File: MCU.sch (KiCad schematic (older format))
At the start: 10 parts, among them J2 Conn_01x02, J5 Conn_02x03_Odd_Even, SW2 SW_SPDT, U3 ATTINY13-20SSU

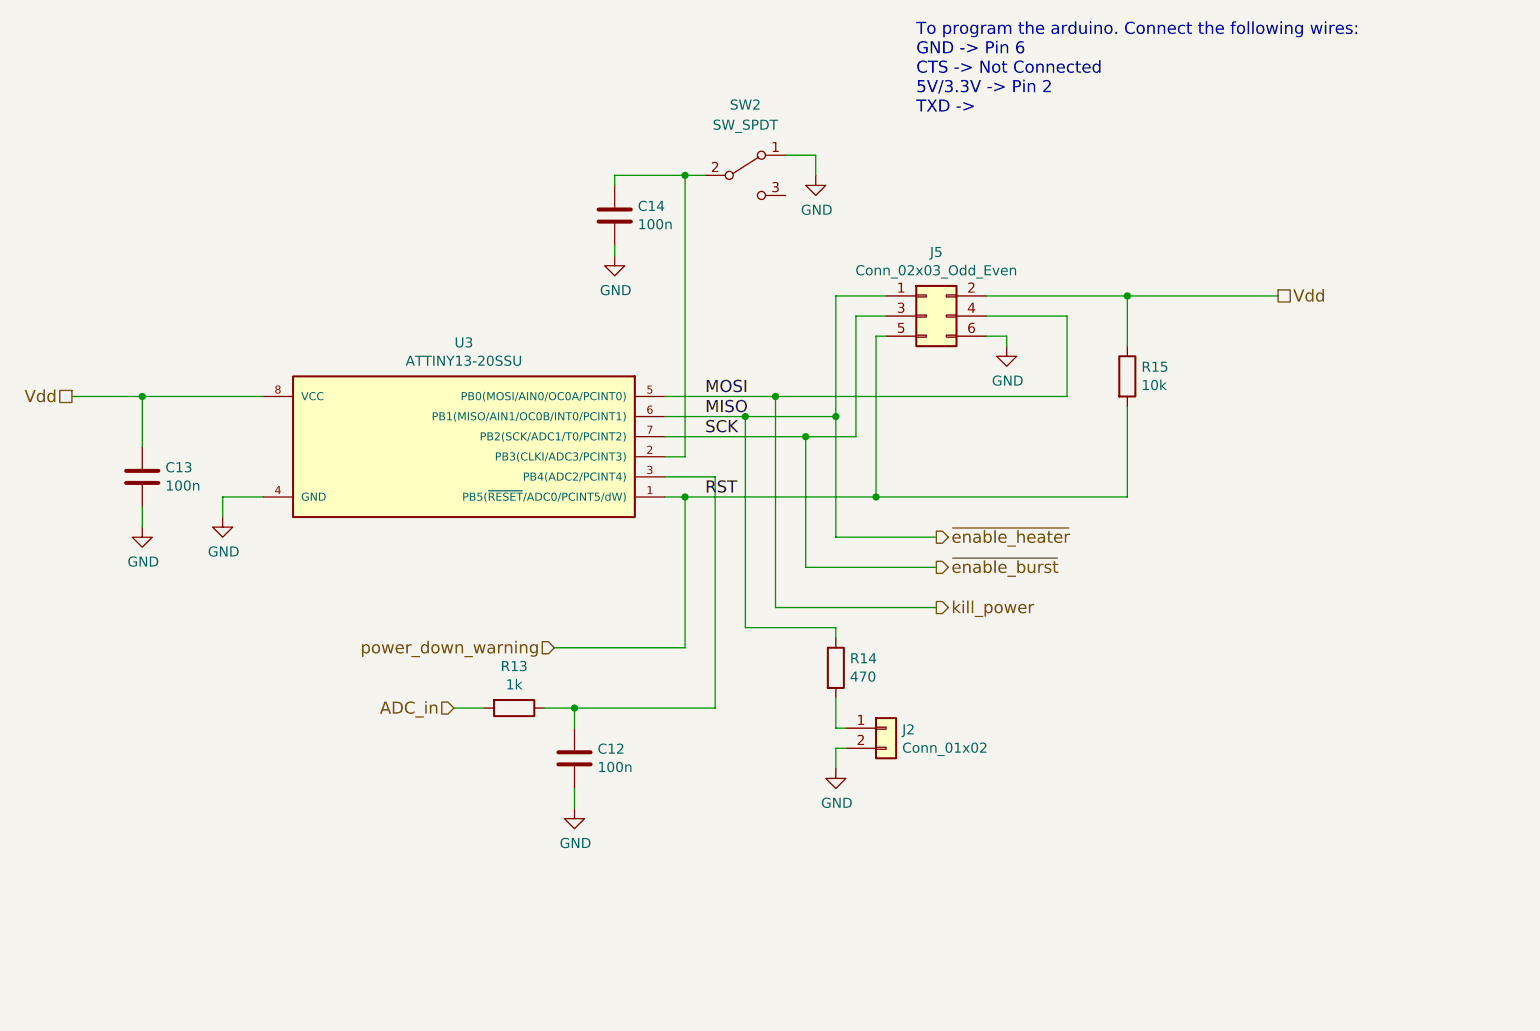
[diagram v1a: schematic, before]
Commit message: Moved MCU pins around to make sure that they do not interfere with the programmer Moved ISP Header closer to the edge of the board to allow easier access with the programmer Added pulldown resistor to the DCD/DC converters enable pin to make sure it stays off in case of failure Added more PDFs of components
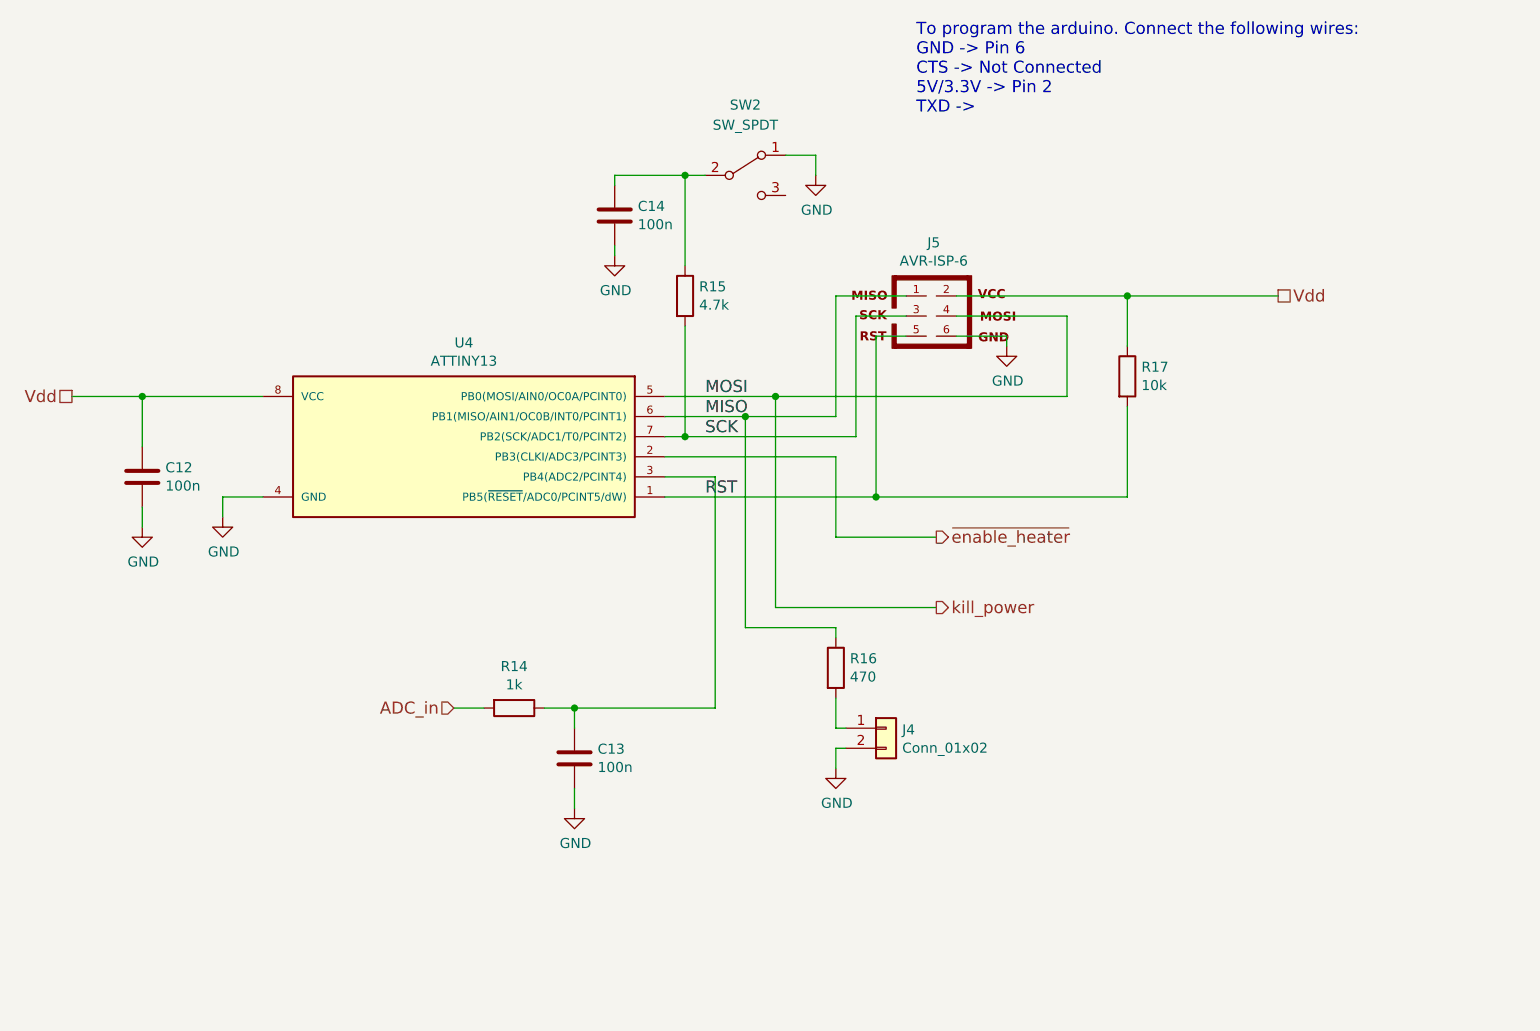
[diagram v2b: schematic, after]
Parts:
- removed J5: Conn_02x03_Odd_Even, Pin_Headers:Pin_Header_Straight_2x03_Pitch2.54mm, symbol Conn_02x03_Odd_Even
- added J5: AVR-ISP-6, Pin_Headers:Pin_Header_Straight_2x03_Pitch2.54mm, symbol AVR-ISP-6
- added R15: 4.7k, Resistors_SMD:R_0603, symbol R
- U4: renamed from U3; value ATTINY13-20SSU -> ATTINY13; MFN (none) -> Microchip Technology; MFP (none) -> ATTINY13A-SS7
- renumbered C13 to C12, C12 to C13, J2 to J4, R13 to R14, R14 to R16, R15 to R17
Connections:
- net GND: now also J5.6
- net Vdd: now also J5.2
- net kill_power: now also J5.4
- net ~enable_heater: now also U4.2 (PB3(CLKI/ADC3/PCINT3)); no longer R16.1, U4.6 (PB1(MISO/AIN1/OC0B/INT0/PCINT1))
- net at C14.1, SW2.2 (B): now also R15.1; no longer U4.2 (PB3(CLKI/ADC3/PCINT3))
- net power_down_warning renamed RST
- net RST: now also J5.5
- net ~enable_burst renamed SCK
- net SCK: now also J5.3, R15.2
- new net MISO: J5.1, R16.1, U4.6 (PB1(MISO/AIN1/OC0B/INT0/PCINT1))
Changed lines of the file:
@@
 ~enable_heater
 $Comp
-L R R13
+L R R14
 U 1 1 59D0B837
 P 5550 4550
-F 0 "R13" V 5343 4550 50  0000 C CNN
+F 0 "R14" V 5343 4550 50  0000 C CNN
 F 1 "1k" V 5434 4550 50  0000 C CNN
 F 2 "Resistors_SMD:R_0603" V 5480 4550 50  0001 C CNN
@@
 $EndComp
 $Comp
-L C C12
+L C C13
 U 1 1 59D0B89F
 P 5850 4800
-F 0 "C12" H 5965 4846 50  0000 L CNN
+F 0 "C13" H 5965 4846 50  0000 L CNN
 F 1 "100n" H 5965 4755 50  0000 L CNN
 F 2 "Capacitors_SMD:C_0603" H 5888 4650 50  0001 C CNN
@@
 $EndComp
 $Comp
-L GND #PWR027
+L GND #PWR028
 U 1 1 59D0B8EA
 P 5850 5050
-F 0 "#PWR027" H 5850 4800 50  0001 C CNN
+F 0 "#PWR028" H 5850 4800 50  0001 C CNN
 F 1 "GND" H 5855 4877 50  0000 C CNN
 F 2 "" H 5850 5050 50  0001 C CNN
@@
 $EndComp
 $Comp
-L ATTINY13-20SSU U3
+L ATTINY13-20SSU U4
 U 1 1 59D0BE2F
 P 5300 3250
-F 0 "U3" H 5300 3767 50  0000 C CNN
-F 1 "ATTINY13-20SSU" H 5300 3676 50  0000 C CNN
+F 0 "U4" H 5300 3767 50  0000 C CNN
+F 1 "ATTINY13" H 5300 3676 50  0000 C CNN
 F 2 "Housings_SOIC:SOIC-8_3.9x4.9mm_Pitch1.27mm" H 5900 3250 50  0001 C CIN
 F 3 "" H 4500 3600 50  0001 C CNN
+F 4 "Microchip Technology" H 5300 3250 60  0001 C CNN "MFN"
+F 5 "ATTINY13A-SS7" H 5300 3250 60  0001 C CNN "MFP"
 	1    5300 3250
 	-1   0    0    -1
 $EndComp
 $Comp
-L GND #PWR028
+L GND #PWR029
 U 1 1 59D0C06D
 P 4100 3600
-F 0 "#PWR028" H 4100 3350 50  0001 C CNN
+F 0 "#PWR029" H 4100 3350 50  0001 C CNN
 F 1 "GND" H 4105 3427 50  0000 C CNN
 F 2 "" H 4100 3600 50  0001 C CNN
@@
 $EndComp
 $Comp
-L Conn_02x03_Odd_Even J5
-U 1 1 59D0C162
-P 7600 2600
-F 0 "J5" H 7650 2917 50  0000 C CNN
-F 1 "Conn_02x03_Odd_Even" H 7650 2826 50  0000 C CNN
-F 2 "Pin_Headers:Pin_Header_Straight_2x03_Pitch2.54mm" H 7600 2600 50  0001 C CNN
-F 3 "" H 7600 2600 50  0001 C CNN
-	1    7600 2600
-	1    0    0    -1
-$EndComp
-$Comp
-L GND #PWR029
+L GND #PWR030
 U 1 1 59D0C22E
 P 8000 2750
-F 0 "#PWR029" H 8000 2500 50  0001 C CNN
+F 0 "#PWR030" H 8000 2500 50  0001 C CNN
 F 1 "GND" H 8005 2577 50  0000 C CNN
 F 2 "" H 8000 2750 50  0001 C CNN
@@
 Vdd
 $Comp
-L R R15
+L R R17
 U 1 1 59D0C448
 P 8600 2900
-F 0 "R15" H 8670 2946 50  0000 L CNN
+F 0 "R17" H 8670 2946 50  0000 L CNN
 F 1 "10k" H 8670 2855 50  0000 L CNN
 F 2 "Resistors_SMD:R_0603" V 8530 2900 50  0001 C CNN
@@
 $EndComp
 $Comp
-L C C13
+L C C12
 U 1 1 59D0C55B
 P 3700 3400
-F 0 "C13" H 3815 3446 50  0000 L CNN
+F 0 "C12" H 3815 3446 50  0000 L CNN
 F 1 "100n" H 3815 3355 50  0000 L CNN
 F 2 "Capacitors_SMD:C_0603" H 3738 3250 50  0001 C CNN
@@
 $EndComp
 $Comp
-L GND #PWR030
+L GND #PWR031
 U 1 1 59D0C561
 P 3700 3650
-F 0 "#PWR030" H 3700 3400 50  0001 C CNN
+F 0 "#PWR031" H 3700 3400 50  0001 C CNN
 F 1 "GND" H 3705 3477 50  0000 C CNN
 F 2 "" H 3700 3650 50  0001 C CNN
@@
 Text HLabel 7650 4050 2    60   Output ~ 0
 kill_power
-Text HLabel 5750 4250 0    60   Input ~ 0
-power_down_warning
-$Comp
-L R R14
+$Comp
+L R R16
 U 1 1 59D0EA56
 P 7150 4350
-F 0 "R14" H 7220 4396 50  0000 L CNN
+F 0 "R16" H 7220 4396 50  0000 L CNN
 F 1 "470" H 7220 4305 50  0000 L CNN
 F 2 "Resistors_SMD:R_0603" V 7080 4350 50  0001 C CNN
@@
 $EndComp
 $Comp
-L GND #PWR031
+L GND #PWR032
 U 1 1 59D0EBB5
 P 7150 4850
-F 0 "#PWR031" H 7150 4600 50  0001 C CNN
+F 0 "#PWR032" H 7150 4600 50  0001 C CNN
 F 1 "GND" H 7155 4677 50  0000 C CNN
 F 2 "" H 7150 4850 50  0001 C CNN
@@
 	1    0    0    -1
 $EndComp
-Text HLabel 7650 3850 2    60   Output ~ 0
-~enable_burst
 $Comp
 L SW_SPDT SW2
@@
 $EndComp
 $Comp
-L GND #PWR032
+L GND #PWR033
 U 1 1 59D11856
 P 7050 1900
-F 0 "#PWR032" H 7050 1650 50  0001 C CNN
+F 0 "#PWR033" H 7050 1650 50  0001 C CNN
 F 1 "GND" H 7055 1727 50  0000 C CNN
 F 2 "" H 7050 1900 50  0001 C CNN
@@
 $EndComp
 $Comp
-L Conn_01x02 J2
+L Conn_01x02 J4
 U 1 1 59D151F1
 P 7400 4650
-F 0 "J2" H 7480 4642 50  0000 L CNN
+F 0 "J4" H 7480 4642 50  0000 L CNN
 F 1 "Conn_01x02" H 7480 4551 50  0000 L CNN
 F 2 "Connectors_JST:JST_PH_B2B-PH-K_02x2.00mm_Straight" H 7400 4650 50  0001 C CNN
@@
 $EndComp
 $Comp
-L GND #PWR033
+L GND #PWR034
 U 1 1 59D1A77F
 P 6050 2300
-F 0 "#PWR033" H 6050 2050 50  0001 C CNN
+F 0 "#PWR034" H 6050 2050 50  0001 C CNN
 F 1 "GND" H 6055 2127 50  0000 C CNN
 F 2 "" H 6050 2300 50  0001 C CNN
@@
 	4100 3500 4100 3600
 Wire Wire Line
-	7400 2500 7150 2500
-Wire Wire Line
-	7150 2500 7150 3700
+	7150 2500 7500 2500
 Wire Wire Line
 	6300 3100 7150 3100
 Wire Wire Line
-	7400 2600 7250 2600
+	7250 2600 7500 2600
 Wire Wire Line
 	7250 2600 7250 3200
@@
 	7250 3200 6300 3200
 Wire Wire Line
-	7400 2700 7350 2700
+	7350 2700 7500 2700
 Wire Wire Line
 	7350 2700 7350 3500
@@
 	8300 3000 8300 2600
 Wire Wire Line
-	8300 2600 7900 2600
-Wire Wire Line
-	7900 2700 8000 2700
+	8300 2600 7750 2600
+Wire Wire Line
+	7750 2700 8000 2700
 Wire Wire Line
 	8000 2700 8000 2750
@@
 Connection ~ 3700 3000
 Wire Wire Line
-	5750 4250 6400 4250
-Wire Wire Line
 	7150 3700 7650 3700
-Connection ~ 7150 3100
 Wire Wire Line
 	6850 4050 7650 4050
@@
 Connection ~ 6700 3100
 Wire Wire Line
-	7000 3200 7000 3850
-Wire Wire Line
-	7000 3850 7650 3850
-Connection ~ 7000 3200
-Wire Wire Line
-	6400 4250 6400 3500
-Connection ~ 6400 3500
-Wire Wire Line
 	6050 1900 6500 1900
 Wire Wire Line
@@
 Connection ~ 6850 3000
 Wire Wire Line
-	6400 1900 6400 3300
-Wire Wire Line
-	6400 3300 6300 3300
-Wire Wire Line
 	7150 4650 7200 4650
 Wire Wire Line
@@
 	6050 2300 6050 2250
 Wire Wire Line
-	7900 2500 9350 2500
+	7750 2500 9350 2500
 Text Label 6500 3500 0    60   ~ 0
 RST
@@
 Text Label 6500 3200 0    60   ~ 0
 SCK
+Wire Wire Line
+	7150 3100 7150 2500
+Wire Wire Line
+	7150 3300 7150 3700
+Wire Wire Line
+	6300 3300 7150 3300
+$Comp
+L R R15
+U 1 1 5A46E3DE
+P 6400 2500
+F 0 "R15" H 6470 2546 50  0000 L CNN
+F 1 "4.7k" H 6470 2455 50  0000 L CNN
+F 2 "Resistors_SMD:R_0603" V 6330 2500 50  0001 C CNN
+F 3 "" H 6400 2500 50  0001 C CNN
+F 4 "Yageo" H 6400 2500 60  0001 C CNN "MFN"
+F 5 "RC0603FR-074K7L" H 6400 2500 60  0001 C CNN "MFP"
+	1    6400 2500
+	1    0    0    -1
+$EndComp
+Wire Wire Line
+	6400 1900 6400 2350
+Wire Wire Line
+	6400 2650 6400 3200
+Connection ~ 6400 3200
+$Comp
+L AVR-ISP-6 J5
+U 1 1 5A46F178
+P 7650 2600
+F 0 "J5" H 7637 2965 50  0000 C CNN
+F 1 "AVR-ISP-6" H 7637 2874 50  0000 C CNN
+F 2 "Pin_Headers:Pin_Header_Straight_2x03_Pitch2.54mm" V 7130 2640 50  0001 C CNN
+F 3 "" H 7625 2600 50  0001 C CNN
+	1    7650 2600
+	1    0    0    -1
+$EndComp
 $EndSCHEMATC

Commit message: Added part names and BOM Added Gerber files
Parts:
- C12, C13, C14: MFN (none) -> Murata; MFP (none) -> GRM188R71H104KA93D
- J4: MFN (none) -> JST; MFP (none) -> B2B-PH-K-S(LF)(SN)
- R14: MFN (none) -> Yageo; MFP (none) -> RC0603FR-071KL
- R16: MFN (none) -> Yageo; MFP (none) -> RC0603FR-07470RL
- R17: MFN (none) -> Yageo; MFP (none) -> RC0603JR-0710KL
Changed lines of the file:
@@
 F 2 "Resistors_SMD:R_0603" V 5480 4550 50  0001 C CNN
 F 3 "" H 5550 4550 50  0001 C CNN
+F 4 "Yageo" H 5550 4550 60  0001 C CNN "MFN"
+F 5 "RC0603FR-071KL" H 5550 4550 60  0001 C CNN "MFP"
 	1    5550 4550
 	0    1    1    0
@@
 F 2 "Capacitors_SMD:C_0603" H 5888 4650 50  0001 C CNN
 F 3 "" H 5850 4800 50  0001 C CNN
+F 4 "Murata" H 5850 4800 60  0001 C CNN "MFN"
+F 5 "GRM188R71H104KA93D" H 5850 4800 60  0001 C CNN "MFP"
 	1    5850 4800
 	1    0    0    -1
@@
 F 2 "Resistors_SMD:R_0603" V 8530 2900 50  0001 C CNN
 F 3 "" H 8600 2900 50  0001 C CNN
+F 4 "Yageo" H 8600 2900 60  0001 C CNN "MFN"
+F 5 "RC0603JR-0710KL" H 8600 2900 60  0001 C CNN "MFP"
 	1    8600 2900
 	1    0    0    -1
@@
 F 2 "Capacitors_SMD:C_0603" H 3738 3250 50  0001 C CNN
 F 3 "" H 3700 3400 50  0001 C CNN
+F 4 "Murata" H 3700 3400 60  0001 C CNN "MFN"
+F 5 "GRM188R71H104KA93D" H 3700 3400 60  0001 C CNN "MFP"
 	1    3700 3400
 	1    0    0    -1
@@
 F 2 "Resistors_SMD:R_0603" V 7080 4350 50  0001 C CNN
 F 3 "" H 7150 4350 50  0001 C CNN
+F 4 "Yageo" H 7150 4350 60  0001 C CNN "MFN"
+F 5 "RC0603FR-07470RL" H 7150 4350 60  0001 C CNN "MFP"
 	1    7150 4350
 	1    0    0    -1
@@
 F 2 "Connectors_JST:JST_PH_B2B-PH-K_02x2.00mm_Straight" H 7400 4650 50  0001 C CNN
 F 3 "" H 7400 4650 50  0001 C CNN
-F 4 "Amber LED" H 7400 4650 60  0001 C CNN "Note"
+F 4 "JST" H 7400 4650 60  0001 C CNN "MFN"
+F 5 "B2B-PH-K-S(LF)(SN)" H 7400 4650 60  0001 C CNN "MFP"
+F 6 "Amber LED" H 7400 4650 60  0001 C CNN "Note"
 	1    7400 4650
 	1    0    0    -1
@@
 F 2 "Capacitors_SMD:C_0603" H 6088 1950 50  0001 C CNN
 F 3 "" H 6050 2100 50  0001 C CNN
+F 4 "Murata" H 6050 2100 60  0001 C CNN "MFN"
+F 5 "GRM188R71H104KA93D" H 6050 2100 60  0001 C CNN "MFP"
 	1    6050 2100
 	1    0    0    -1
